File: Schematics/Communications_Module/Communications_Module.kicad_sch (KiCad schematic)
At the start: 50 parts, among them J1 USB_B_Micro, J2 Bus_PCI_Express_x1, J3 Conn_01x04_Pin, Q1 NMOS, SW1 Boot Mode, U1 RFM95W-915S2, U2 W25Q128JVSIQ, U3 AMS1117-3.3, U4 LM66100DCKR, U5 LM66100DCKR, U6 LM66100DCKR, U7 STM32F103CBTx, U8 ACS706xLC-05C, U9 ISO1042BQDWVQ1, Y1 X322516MMB4SI

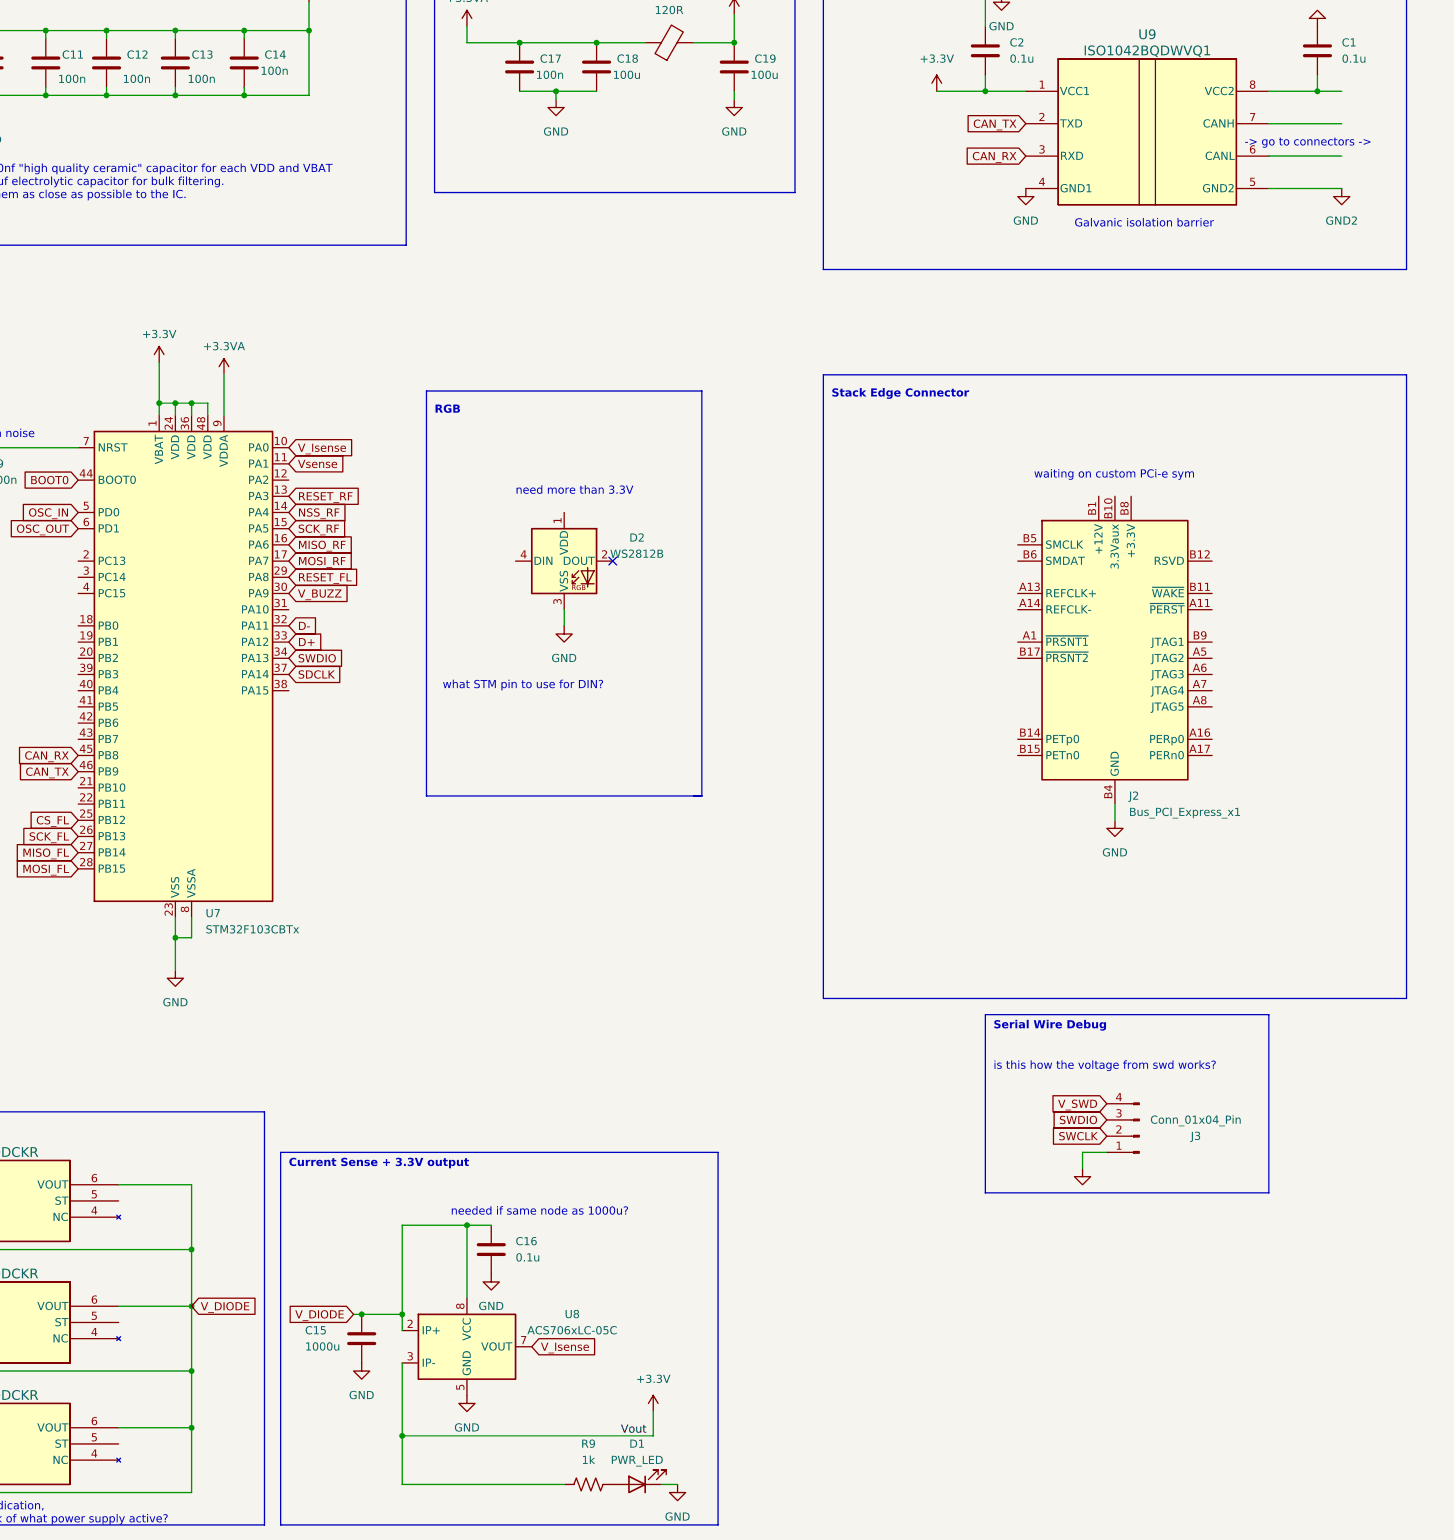
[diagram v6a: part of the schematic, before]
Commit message: Added custom edge connector symbol to project
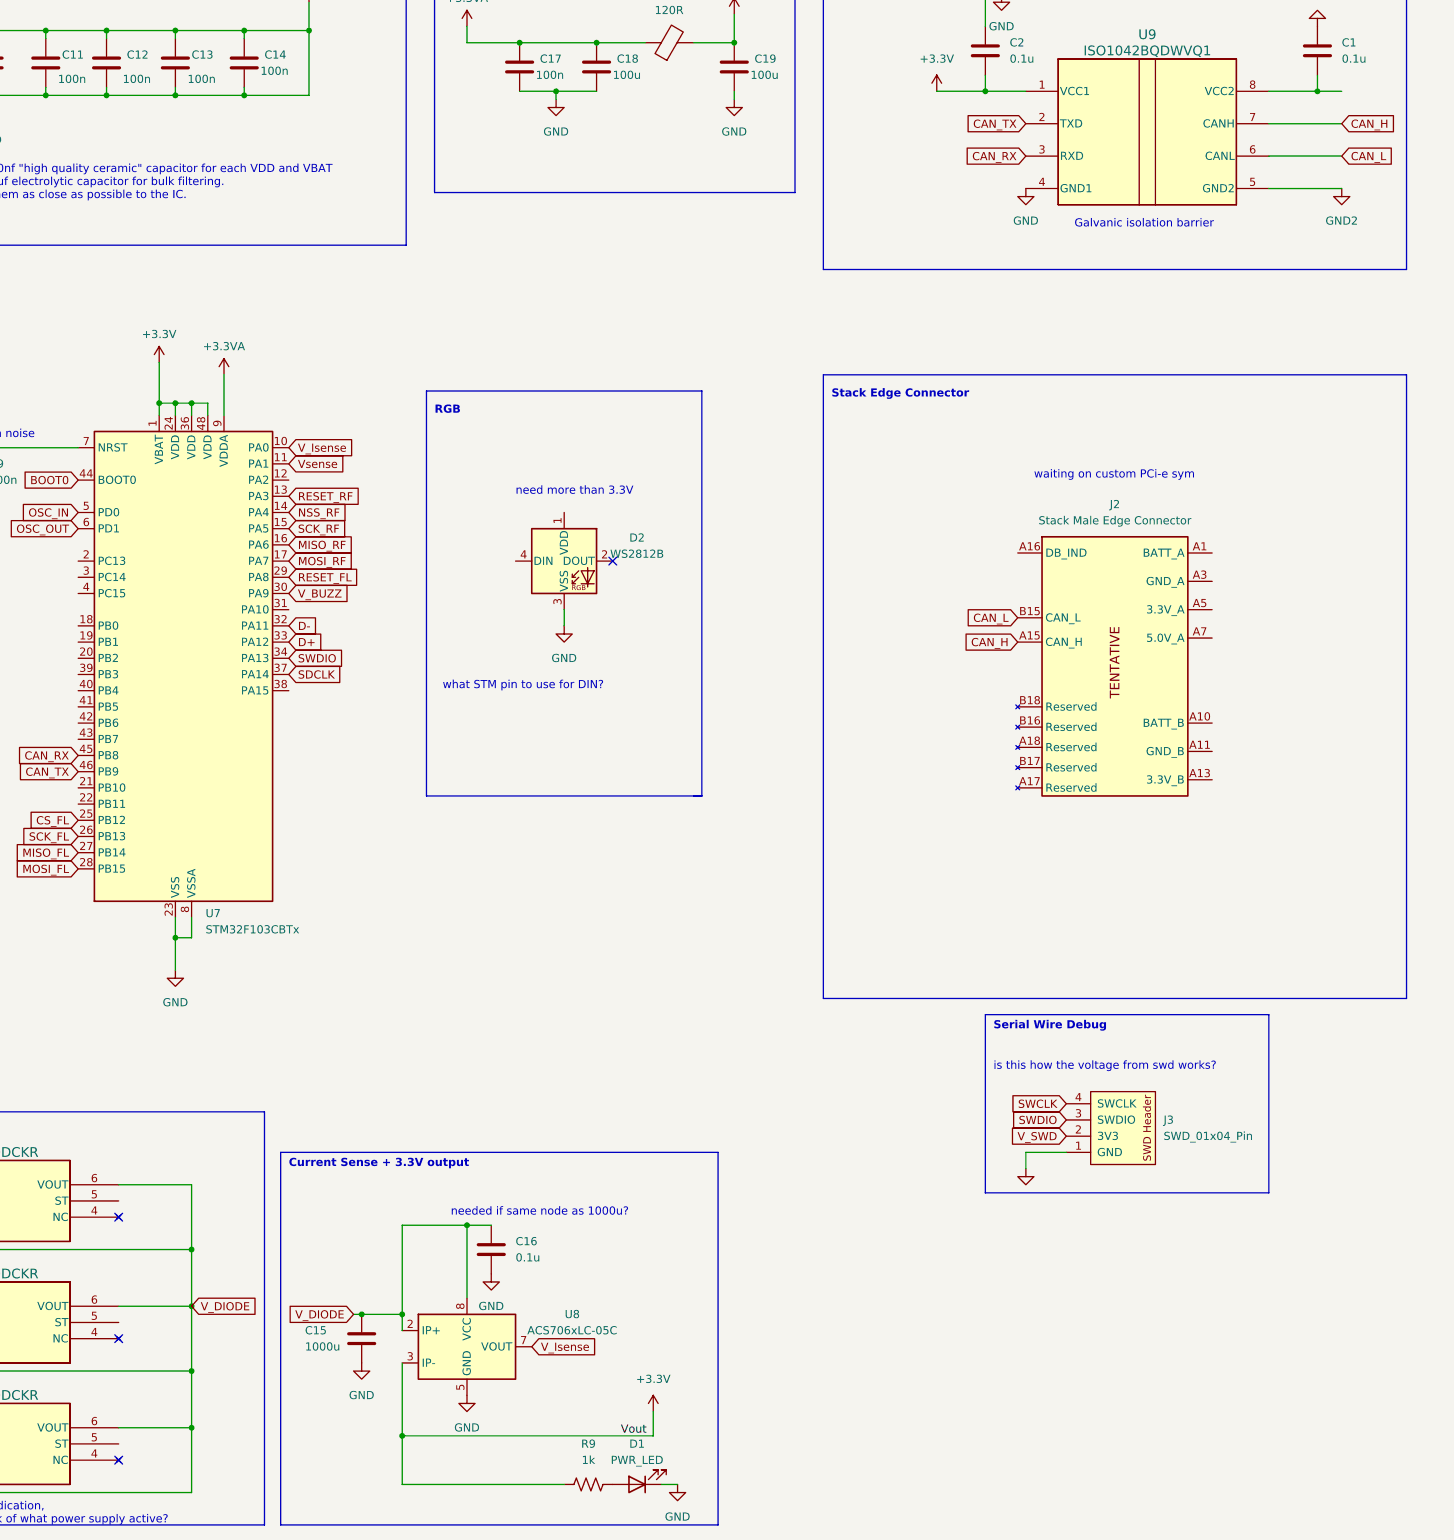
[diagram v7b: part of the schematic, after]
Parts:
- removed J2: Bus_PCI_Express_x1, symbol Connector:Bus_PCI_Express_x1
- removed J3: Conn_01x04_Pin, symbol Connector:Conn_01x04_Pin
- added J2: Stack Male Edge Connector, Connector_PCBEdge:BUS_PCIexpress_x1, symbol QRET_Edge_Connector:Stack Male Edge Connector
- added J3: SWD_01x04_Pin, SWD_Header:SWD_PinHeader_1x04_P2.54mm_Horizontal, symbol QRET_Edge_Connector:SWD_01x04_Pin
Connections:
- net +3.3V: now also J3.1 (GND)
- net SWCLK: now also J3.4 (SWCLK)
- net SWDIO: now also J3.3 (SWDIO)
- net V_SWD: now also J3.2 (3V3)
- net CAN_L: now reaches U9.6 (CANL)
- net CAN_L: now also J2.B15 (CAN_L)
- net CAN_H: now reaches U9.7 (CANH)
- net CAN_H: now also J2.A15 (CAN_H)
- new net: J2.A1 (BATT_A), J2.A2 (BATT_A), J2.B1 (BATT_A), J2.B2 (BATT_A)
- new net: J2.A10 (BATT_B), J2.A9 (BATT_B), J2.B10 (BATT_B), J2.B9 (BATT_B)
- new net: J2.A11 (GND_B), J2.A12 (GND_B), J2.A14 (GND_B), J2.B11 (GND_B), J2.B12 (GND_B), J2.B14 (GND_B)
- new net: J2.A13 (3.3V_B), J2.B13 (3.3V_B)
- new net: J2.A3 (GND_A), J2.A4 (GND_A), J2.A6 (GND_A), J2.A8 (GND_A), J2.B3 (GND_A), J2.B4 (GND_A), J2.B6 (GND_A), J2.B8 (GND_A)
- new net: J2.A5 (3.3V_A), J2.B5 (3.3V_A)
- new net: J2.A7 (5.0V_A), J2.B7 (5.0V_A)
- no-connect marks 3 -> 6
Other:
- note removed: "-> go to connectors ->"

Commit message: A few small changes
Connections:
- net +3.3V: now also J2.A3 (GND_A), J2.A4 (GND_A), J2.A6 (GND_A), J2.A8 (GND_A), J2.B3 (GND_A), J2.B4 (GND_A), J2.B6 (GND_A), J2.B8 (GND_A)
- net +5V: now reaches C1.2, U9.8 (VCC2)
- net +5V: now also J2.A7 (5.0V_A), J2.B7 (5.0V_A)
- net RGB: now reaches D2.4 (DIN)
- no-connect marks 6 -> 11
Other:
- note added: "need more than 3.3V?"
- note added: "screw isolation?"
- note removed: "can u use the same pullup?"
- note removed: "is this how the voltage from swd works?"
- note removed: "need more than 3.3V"
- note removed: "waiting on custom PCi-e sym"
- moved on the sheet: J2
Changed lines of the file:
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@@
   (title_block
     (title "QRET 23-24 SRAD Communications Module")
-    (date "2024-02-02")
-    (rev "V0.2.3")
+    (date "2024-02-15")
+    (rev "V0.2.4")
     (company "Queen's Rocket Engineering Team")
     (comment 1 "Contributors: Oak Campbell")
@@
   (junction (at 170.18 238.76) (diameter 0) (color 0 0 0 0)
   )
+  (no_connect (at 356.87 147.32))
   (no_connect (at 215.9 217.17))
+  (no_connect (at 356.87 137.16))
   (no_connect (at 293.37 114.3))
+  (no_connect (at 356.87 142.24))
   (no_connect (at 215.9 236.22))
   (no_connect (at 104.14 237.49))
   (no_connect (at 114.3 232.41))
   (no_connect (at 215.9 255.27))
+  (no_connect (at 356.87 139.7))
+  (no_connect (at 356.87 144.78))
   (wire (pts (xy 260.35 218.44) (xy 270.51 218.44))
     (stroke (width 0) (type default))
@@
     (stroke (width 0) (type default))
   )
+  (wire (pts (xy 403.86 119.38) (xy 403.86 120.65))
+    (stroke (width 0) (type default))
+  )
   (wire (pts (xy 55.88 80.01) (xy 58.42 80.01))
     (stroke (width 0) (type default))
@@
     (stroke (width 0) (type default))
   )
+  (wire (pts (xy 387.35 128.27) (xy 392.43 128.27))
+    (stroke (width 0) (type default))
+  )
   (polyline (pts (xy 83.82 96.52) (xy 83.82 151.13))
     (stroke (width 0) (type default))
@@
     (stroke (width 0) (type default))
   )
+  (wire (pts (xy 392.43 127) (xy 392.43 128.27))
+    (stroke (width 0) (type default))
+  )
   (wire (pts (xy 46.99 180.34) (xy 46.99 181.61))
     (stroke (width 0) (type default))
@@
     (stroke (width 0) (type default))
   )
+  (wire (pts (xy 387.35 119.38) (xy 403.86 119.38))
+    (stroke (width 0) (type default))
+  )
   (wire (pts (xy 351.79 25.4) (xy 354.33 25.4))
     (stroke (width 0) (type default))
@@
     (stroke (width 0) (type default))
   )
+  (wire (pts (xy 415.29 39.37) (xy 415.29 40.64))
+    (stroke (width 0) (type default))
+  )
   (wire (pts (xy 285.75 259.08) (xy 260.35 259.08))
     (stroke (width 0) (type default))
@@
     (stroke (width 0) (type default))
   )
-  (wire (pts (xy 403.86 40.64) (xy 407.67 40.64))
+  (wire (pts (xy 403.86 40.64) (xy 415.29 40.64))
     (stroke (width 0) (type default))
   )
@@
     (stroke (width 0) (type default))
   )
+  (wire (pts (xy 285.75 104.14) (xy 285.75 106.68))
+    (stroke (width 0) (type default))
+  )
   (polyline (pts (xy 15.24 93.98) (xy 15.24 39.37))
     (stroke (width 0) (type default))
@@
     (effects (font (size 1.27 1.27)) (justify left bottom))
   )
-  (text "can u use the same pullup?" (at 16.51 115.57 0)
-    (effects (font (size 1.27 1.27)) (justify left bottom))
-  )
   (text "Cap to prevent resets from noise" (at 173.99 95.25 0)
     (effects (font (size 1.27 1.27)) (justify left bottom))
@@
     (effects (font (size 1.27 1.27) (thickness 0.254) bold) (justify left bottom))
   )
-  (text "need more than 3.3V" (at 278.13 104.14 0)
+  (text "need more than 3.3V?" (at 278.13 95.25 0)
     (effects (font (size 1.27 1.27)) (justify left bottom))
   )
@@
     (effects (font (size 1.27 1.27) (thickness 0.254) bold) (justify left bottom))
   )
+  (text "screw isolation?" (at 287.02 102.87 0)
+    (effects (font (size 1.27 1.27)) (justify left bottom))
+  )
   (text "One 100nf \"high quality ceramic\" capacitor for each VDD and VBAT\nOne 10uf electrolytic capacitor for bulk filtering.\nPlace them as close as possible to the IC."
     (at 190.5 57.785 0)
@@
     (effects (font (size 1.27 1.27)) (justify left bottom))
   )
+  (text "screw isolation?" (at 400.05 64.77 0)
+    (effects (font (size 1.27 1.27)) (justify left bottom))
+  )
   (text "No ic2 uses SPI instead" (at 22.86 53.34 0)
     (effects (font (size 1.27 1.27)) (justify left bottom))
@@
     (effects (font (size 1.27 1.27)) (justify left bottom))
   )
-  (text "waiting on custom PCi-e sym" (at 359.41 101.6 0)
-    (effects (font (size 1.27 1.27)) (justify left bottom))
-  )
   (text "what voltage here?" (at 36.83 165.1 0)
     (effects (font (size 1.27 1.27)) (justify left bottom))
@@
     (effects (font (size 1.27 1.27)) (justify left bottom))
   )
-  (text "is this how the voltage from swd works?" (at 353.06 194.31 0)
-    (effects (font (size 1.27 1.27)) (justify left bottom))
-  )
   (text "Boot Mode" (at 62.23 15.875 0)
     (effects (font (size 1.27 1.27) (thickness 0.254) bold) (justify left bottom))
@@
     )
   )
+  (global_label "RGB" (shape input) (at 278.13 114.3 180) (fields_autoplaced)
+    (effects (font (size 1.27 1.27)) (justify right))
+    (property "Intersheetrefs" "${INTERSHEET_REFS}" (at 271.3348 114.3 0)
+      (effects (font (size 1.27 1.27)) (justify right) hide)
+    )
+  )
   (global_label "V_SWD" (shape input) (at 364.49 204.47 180) (fields_autoplaced)
     (effects (font (size 1.27 1.27)) (justify right))
@@
     )
   )
-  (global_label "CAN_H" (shape input) (at 356.87 127 180) (fields_autoplaced)
+  (global_label "CAN_H" (shape input) (at 356.87 128.27 180) (fields_autoplaced)
     (effects (font (size 1.27 1.27)) (justify right))
-    (property "Intersheetrefs" "${INTERSHEET_REFS}" (at 347.8976 127 0)
+    (property "Intersheetrefs" "${INTERSHEET_REFS}" (at 347.8976 128.27 0)
       (effects (font (size 1.27 1.27)) (justify right) hide)
     )
@@
     )
   )
-  (global_label "CAN_L" (shape input) (at 356.87 123.19 180) (fields_autoplaced)
+  (global_label "CAN_L" (shape input) (at 356.87 124.46 180) (fields_autoplaced)
     (effects (font (size 1.27 1.27)) (justify right))
-    (property "Intersheetrefs" "${INTERSHEET_REFS}" (at 348.2 123.19 0)
+    (property "Intersheetrefs" "${INTERSHEET_REFS}" (at 348.2 124.46 0)
       (effects (font (size 1.27 1.27)) (justify right) hide)
     )
@@
     )
   )
+  (symbol (lib_id "power:GND") (at 403.86 120.65 0) (unit 1)
+    (in_bom yes) (on_board yes) (dnp no) (fields_autoplaced)
+    (property "Reference" "#PWR037" (at 403.86 127 0)
+      (effects (font (size 1.27 1.27)) hide)
+    )
+    (property "Value" "GND" (at 403.86 125.73 0)
+      (effects (font (size 1.27 1.27)))
+    )
+    (property "Footprint" "" (at 403.86 120.65 0)
+      (effects (font (size 1.27 1.27)) hide)
+    )
+    (property "Datasheet" "" (at 403.86 120.65 0)
+      (effects (font (size 1.27 1.27)) hide)
+    )
+    (pin "1")
+    (instances
+      (project "Communications_Module"
+        (path "/ace06731-9b48-45c3-868d-c65fed1a8f9b"
+          (reference "#PWR037") (unit 1)
+        )
+      )
+    )
+  )
   (symbol (lib_id "QRET_Buck_PSU:LM66100DCKR") (at 195.58 252.73 0) (unit 1)
     (in_bom yes) (on_board yes) (dnp no)
@@
     )
   )
+  (symbol (lib_id "power:+5V") (at 392.43 127 0) (unit 1)
+    (in_bom yes) (on_board yes) (dnp no) (fields_autoplaced)
+    (property "Reference" "#PWR042" (at 392.43 130.81 0)
+      (effects (font (size 1.27 1.27)) hide)
+    )
+    (property "Value" "+5V" (at 392.43 121.92 0)
+      (effects (font (size 1.27 1.27)))
+    )
+    (property "Footprint" "" (at 392.43 127 0)
+      (effects (font (size 1.27 1.27)) hide)
+    )
+    (property "Datasheet" "" (at 392.43 127 0)
+      (effects (font (size 1.27 1.27)) hide)
+    )
+    (pin "1")
+    (instances
+      (project "Communications_Module"
+        (path "/ace06731-9b48-45c3-868d-c65fed1a8f9b"
+          (reference "#PWR042") (unit 1)
+        )
+      )
+    )
+  )
   (symbol (lib_id "QRET_Edge_Connector:Stack Male Edge Connector") (at 372.11 132.08 0) (unit 1)
     (in_bom yes) (on_board yes) (dnp no) (fields_autoplaced)
@@
     )
   )
+  (symbol (lib_id "power:+5V") (at 285.75 102.87 0) (unit 1)
+    (in_bom yes) (on_board yes) (dnp no) (fields_autoplaced)
+    (property "Reference" "#PWR045" (at 285.75 106.68 0)
+      (effects (font (size 1.27 1.27)) hide)
+    )
+    (property "Value" "+5V" (at 285.75 97.79 0)
+      (effects (font (size 1.27 1.27)))
+    )
+    (property "Footprint" "" (at 285.75 102.87 0)
+      (effects (font (size 1.27 1.27)) hide)
+    )
+    (property "Datasheet" "" (at 285.75 102.87 0)
+      (effects (font (size 1.27 1.27)) hide)
+    )
+    (pin "1")
+    (instances
+      (project "Communications_Module"
+        (path "/ace06731-9b48-45c3-868d-c65fed1a8f9b"
+          (reference "#PWR045") (unit 1)
+        )
+      )
+    )
+  )
   (symbol (lib_id "Switch:SW_SPDT") (at 96.52 27.305 180) (unit 1)
     (in_bom yes) (on_board yes) (dnp no)
@@
     )
   )
+  (symbol (lib_id "power:GND") (at 403.86 57.15 0) (unit 1)
+    (in_bom yes) (on_board yes) (dnp no) (fields_autoplaced)
+    (property "Reference" "#PWR044" (at 403.86 63.5 0)
+      (effects (font (size 1.27 1.27)) hide)
+    )
+    (property "Value" "GND" (at 403.86 62.23 0)
+      (effects (font (size 1.27 1.27)))
+    )
+    (property "Footprint" "" (at 403.86 57.15 0)
+      (effects (font (size 1.27 1.27)) hide)
+    )
+    (property "Datasheet" "" (at 403.86 57.15 0)
+      (effects (font (size 1.27 1.27)) hide)
+    )
+    (pin "1")
+    (instances
+      (project "Communications_Module"
+        (path "/ace06731-9b48-45c3-868d-c65fed1a8f9b"
+          (reference "#PWR044") (unit 1)
+        )
+      )
+    )
+  )
   (symbol (lib_id "power:GND") (at 358.14 209.55 0) (unit 1)
     (in_bom yes) (on_board yes) (dnp no) (fields_autoplaced)
@@
         )
       )
+    )
+  )
+  (symbol (lib_id "power:+5V") (at 415.29 39.37 0) (unit 1)
+    (in_bom yes) (on_board yes) (dnp no) (fields_autoplaced)
+    (property "Reference" "#PWR043" (at 415.29 43.18 0)
+      (effects (font (size 1.27 1.27)) hide)
+    )
+    (property "Value" "+5V" (at 415.29 34.29 0)
+      (effects (font (size 1.27 1.27)))
+    )
+    (property "Footprint" "" (at 415.29 39.37 0)
+      (effects (font (size 1.27 1.27)) hide)
+    )
+    (property "Datasheet" "" (at 415.29 39.37 0)
+      (effects (font (size 1.27 1.27)) hide)
+    )
+    (pin "1")
+    (instances
+      (project "Communications_Module"
+        (path "/ace06731-9b48-45c3-868d-c65fed1a8f9b"
+          (reference "#PWR043") (unit 1)
+        )
+      )
